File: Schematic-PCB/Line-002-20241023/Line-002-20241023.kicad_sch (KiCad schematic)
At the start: 212 parts, among them J1 ICSP, SW1 RESET, U45 ATmega2560-16A, Y1 16MHz

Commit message: add: update: ラインセンサ基板の外形の更新版を追加 & PCBデザイン/回路図を進めた
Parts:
- added C8: 1000uF, Capacitor_SMD:C_0603_1608Metric, symbol Device:C_Small
- added D56: PWR, LED_SMD:LED_0603_1608Metric, symbol Device:LED_Small_Filled
- added J2: VIN, Connector_JST:JST_VH_B2P-VH-B_1x02_P3.96mm_Vertical, symbol Connector:Conn_01x02_Pin
- added R91: 330, Resistor_SMD:R_0603_1608Metric, symbol Device:R_Small
- C1: renamed from C8; footprint (none) -> Capacitor_SMD:C_0603_1608Metric
- C2: renamed from C1; footprint (none) -> Capacitor_SMD:C_0603_1608Metric
- C3: renamed from C2; footprint (none) -> Capacitor_SMD:C_0603_1608Metric
- C4: renamed from C3; footprint (none) -> Capacitor_SMD:C_0603_1608Metric
- C5: renamed from C4; footprint (none) -> Capacitor_SMD:C_0603_1608Metric
- C6: renamed from C5; footprint (none) -> Capacitor_SMD:C_0603_1608Metric
- C7: renamed from C6; footprint (none) -> Capacitor_SMD:C_0603_1608Metric
- C9: renamed from C7; footprint (none) -> Capacitor_SMD:C_0805_2012Metric
- J1: footprint (none) -> Connector_PinHeader_2.54mm:PinHeader_2x03_P2.54mm_Vertical
- JP1, JP2, JP3: footprint (none) -> Jumper:SolderJumper-2_P1.3mm_Open_Pad1.0x1.5mm
- R25, R26, R27, R28: footprint (none) -> Resistor_SMD:R_0603_1608Metric
- R82: renamed from R98; footprint (none) -> Resistor_SMD:R_0603_1608Metric
- R86: renamed from R102; footprint (none) -> Resistor_SMD:R_0603_1608Metric
- R87: renamed from R103; footprint (none) -> Resistor_SMD:R_0603_1608Metric
- R88: renamed from R104; footprint (none) -> Resistor_SMD:R_0603_1608Metric
- R89: renamed from R105; footprint (none) -> Resistor_SMD:R_0603_1608Metric
- R90: renamed from R106; footprint (none) -> Resistor_SMD:R_0603_1608Metric
- Y1: footprint (none) -> @2024TOINIOT2-Line:AL4BT
- renumbered R45 to R29, R46 to R30, R47 to R31, R48 to R32, R49 to R33, R50 to R34, R51 to R35, R52 to R36, R53 to R37, R54 to R38, R55 to R39, R56 to R40, R57 to R41, R58 to R42, R59 to R43, R60 to R44, R61 to R45, R62 to R46, R63 to R47, R64 to R48, R65 to R49, R66 to R50, R67 to R51, R68 to R52, R69 to R53, R70 to R54, R71 to R55, R72 to R56, R73 to R57, R74 to R58, R75 to R59, R76 to R60, R77 to R61, R78 to R62, R79 to R63, R80 to R64, R81 to R65, R82 to R66, R83 to R67, R84 to R68, R85 to R69, R86 to R70, R87 to R71, R88 to R72, R89 to R73, R90 to R74, R91 to R75, R92 to R76, R93 to R77, R94 to R78, R95 to R79, R96 to R80, R97 to R81, R99 to R83, R100 to R84, R101 to R85
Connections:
- net +5V: now also C8.1, J2.1 (Pin_1), R91.2
- net GND: now also C8.2, D56.1 (K), J2.2 (Pin_2)
- new net: D56.2 (A), R91.1

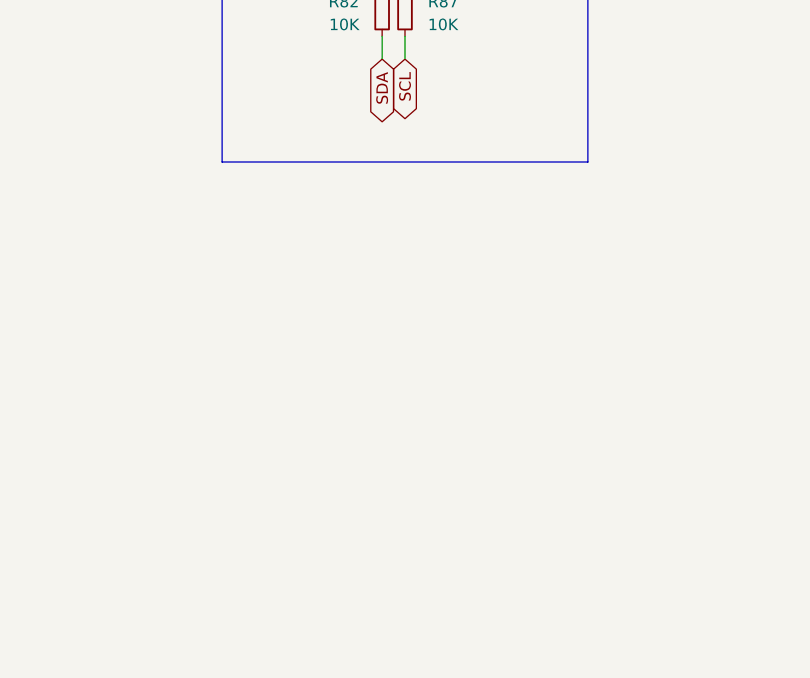
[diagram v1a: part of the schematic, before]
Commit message: update: ラインセンサ基板ver.002を更新した
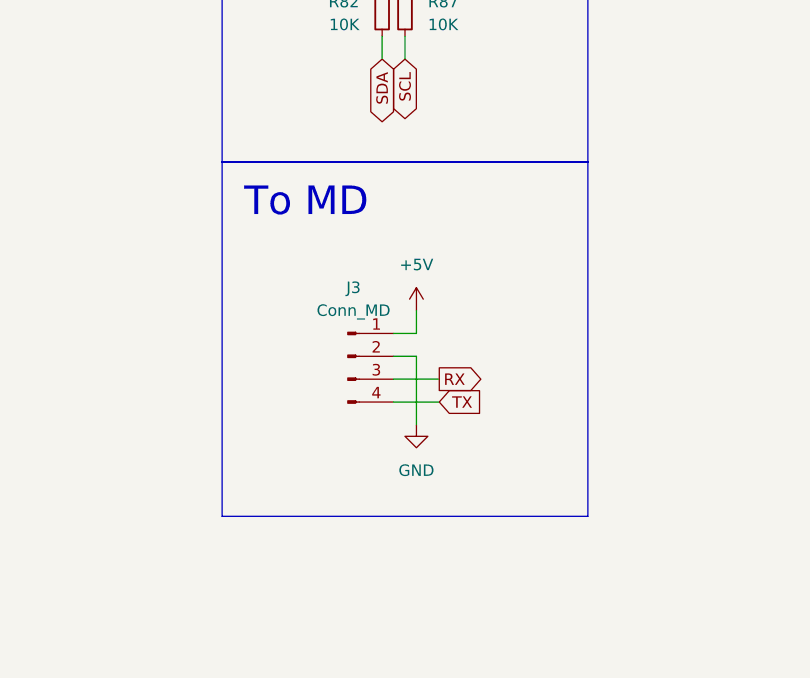
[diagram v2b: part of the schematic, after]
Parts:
- added J3: Conn_MD, symbol Connector:Conn_01x04_Pin
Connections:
- net +5V: now also J3.1 (Pin_1)
- net GND: now also J3.2 (Pin_2)
- new net RX: J3.3 (Pin_3)
- new net TX: J3.4 (Pin_4)
